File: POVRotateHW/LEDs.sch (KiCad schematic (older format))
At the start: 8 parts

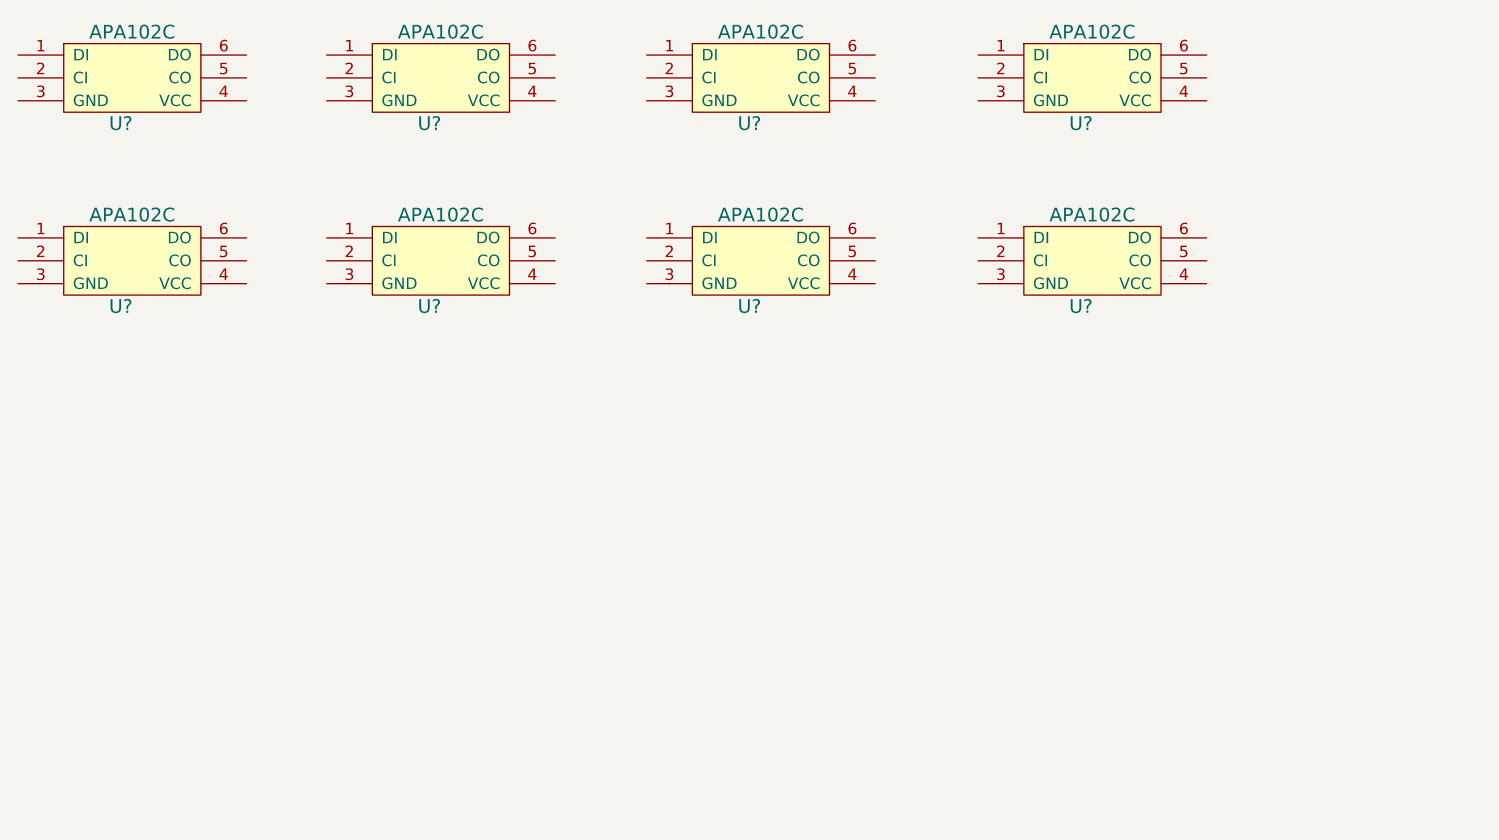
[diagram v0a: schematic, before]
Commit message: Connected some pins up.
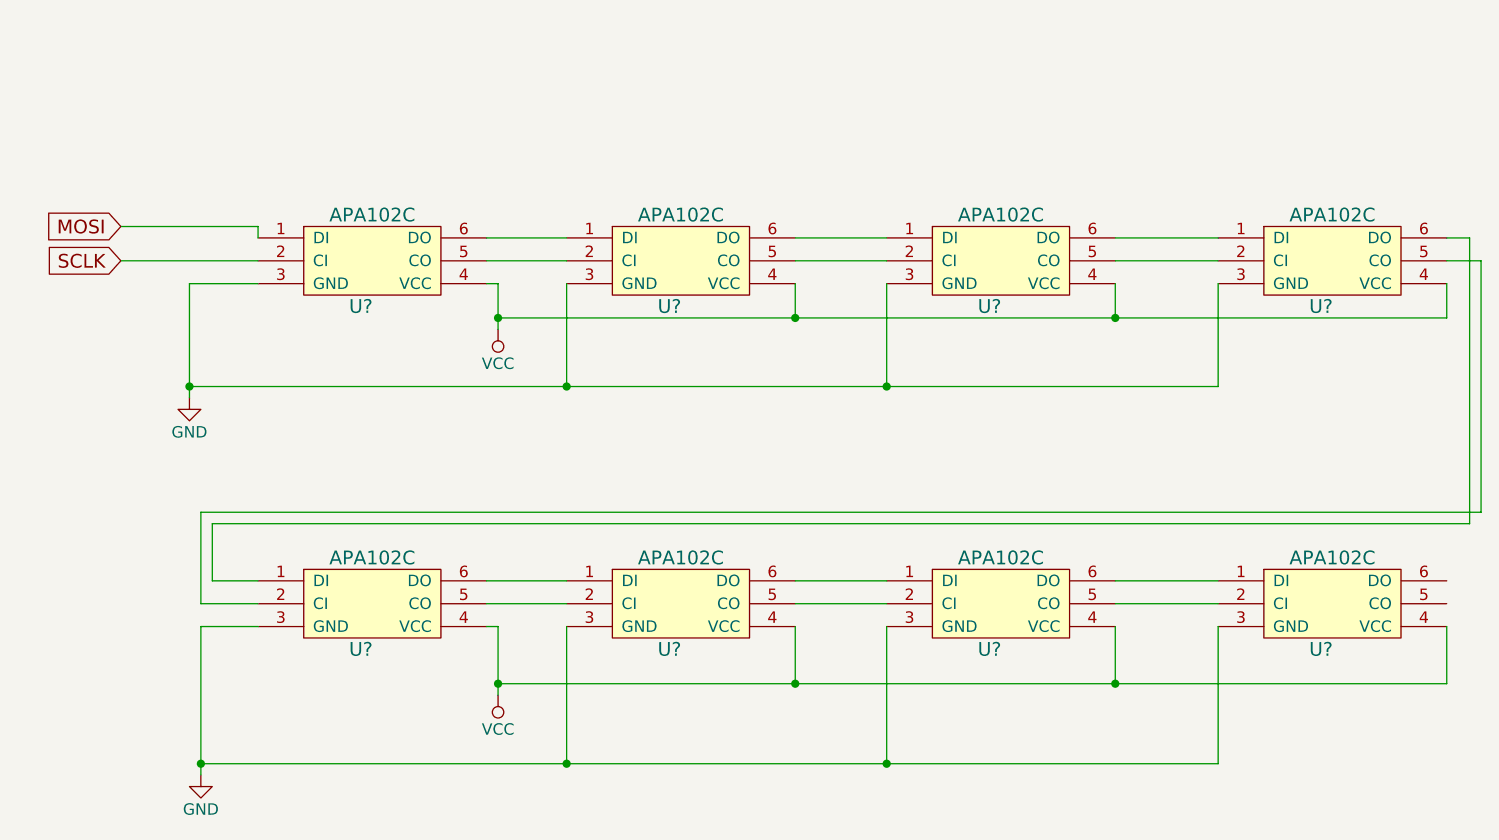
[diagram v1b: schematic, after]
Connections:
- net MOSI: now reaches U?.1 (DI)
- net SCLK: now reaches U?.2 (CI)
- net GND: now reaches U?.3 (GND)
- net GND: now also U?.3 (GND), U?.3 (GND), U?.3 (GND), U?.3 (GND), U?.3 (GND), U?.3 (GND), U?.3 (GND)
- net VCC: now reaches U?.4 (VCC)
- net VCC: now also U?.4 (VCC), U?.4 (VCC), U?.4 (VCC), U?.4 (VCC), U?.4 (VCC), U?.4 (VCC), U?.4 (VCC)
- net at U?.5 (CO): now also U?.2 (CI) (x7)
- net at U?.6 (DO): now also U?.1 (DI) (x7)
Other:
- moved on the sheet: U?

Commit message: Finished the schematic for the POVRotate system, started on layout.
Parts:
- gave numbers to parts that had none: 8
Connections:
- no-connect marks 0 -> 2
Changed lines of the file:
@@
 $EndDescr
 $Comp
-L APA102C U?
+L APA102C U5
 U 1 1 58127307
 P 4300 2700
-F 0 "U?" H 4250 2500 60  0000 C CNN
+F 0 "U5" H 4250 2500 60  0000 C CNN
 F 1 "APA102C" H 4300 2900 60  0000 C CNN
 F 2 "" H 4350 2650 60  0001 C CNN
@@
 $EndComp
 $Comp
-L APA102C U?
+L APA102C U7
 U 1 1 58127369
 P 5650 2700
-F 0 "U?" H 5600 2500 60  0000 C CNN
+F 0 "U7" H 5600 2500 60  0000 C CNN
 F 1 "APA102C" H 5650 2900 60  0000 C CNN
 F 2 "" H 5700 2650 60  0001 C CNN
@@
 $EndComp
 $Comp
-L APA102C U?
+L APA102C U9
 U 1 1 581273A7
 P 7050 2700
-F 0 "U?" H 7000 2500 60  0000 C CNN
+F 0 "U9" H 7000 2500 60  0000 C CNN
 F 1 "APA102C" H 7050 2900 60  0000 C CNN
 F 2 "" H 7100 2650 60  0001 C CNN
@@
 $EndComp
 $Comp
-L APA102C U?
+L APA102C U11
 U 1 1 581273F0
 P 8500 2700
-F 0 "U?" H 8450 2500 60  0000 C CNN
+F 0 "U11" H 8450 2500 60  0000 C CNN
 F 1 "APA102C" H 8500 2900 60  0000 C CNN
 F 2 "" H 8550 2650 60  0001 C CNN
@@
 $EndComp
 $Comp
-L APA102C U?
+L APA102C U6
 U 1 1 58127436
 P 4300 4200
-F 0 "U?" H 4250 4000 60  0000 C CNN
+F 0 "U6" H 4250 4000 60  0000 C CNN
 F 1 "APA102C" H 4300 4400 60  0000 C CNN
 F 2 "" H 4350 4150 60  0001 C CNN
@@
 $EndComp
 $Comp
-L APA102C U?
+L APA102C U8
 U 1 1 581274C5
 P 5650 4200
-F 0 "U?" H 5600 4000 60  0000 C CNN
+F 0 "U8" H 5600 4000 60  0000 C CNN
 F 1 "APA102C" H 5650 4400 60  0000 C CNN
 F 2 "" H 5700 4150 60  0001 C CNN
@@
 $EndComp
 $Comp
-L APA102C U?
+L APA102C U10
 U 1 1 5812751F
 P 7050 4200
-F 0 "U?" H 7000 4000 60  0000 C CNN
+F 0 "U10" H 7000 4000 60  0000 C CNN
 F 1 "APA102C" H 7050 4400 60  0000 C CNN
 F 2 "" H 7100 4150 60  0001 C CNN
@@
 $EndComp
 $Comp
-L APA102C U?
+L APA102C U12
 U 1 1 58127568
 P 8500 4200
-F 0 "U?" H 8450 4000 60  0000 C CNN
+F 0 "U12" H 8450 4000 60  0000 C CNN
 F 1 "APA102C" H 8500 4400 60  0000 C CNN
 F 2 "" H 8550 4150 60  0001 C CNN
@@
 SCLK
 $Comp
-L VCC #PWR?
+L VCC #PWR032
 U 1 1 5814D242
 P 4850 3000
-F 0 "#PWR?" H 4850 2850 50  0001 C CNN
+F 0 "#PWR032" H 4850 2850 50  0001 C CNN
 F 1 "VCC" H 4850 3150 50  0000 C CNN
 F 2 "" H 4850 3000 50  0000 C CNN
@@
 $EndComp
 $Comp
-L GND #PWR?
+L GND #PWR033
 U 1 1 5814D248
 P 3500 3300
-F 0 "#PWR?" H 3500 3050 50  0001 C CNN
+F 0 "#PWR033" H 3500 3050 50  0001 C CNN
 F 1 "GND" H 3500 3150 50  0000 C CNN
 F 2 "" H 3500 3300 50  0000 C CNN
@@
 $EndComp
 $Comp
-L GND #PWR?
+L GND #PWR034
 U 1 1 5814D2A4
 P 3550 4950
-F 0 "#PWR?" H 3550 4700 50  0001 C CNN
+F 0 "#PWR034" H 3550 4700 50  0001 C CNN
 F 1 "GND" H 3550 4800 50  0000 C CNN
 F 2 "" H 3550 4950 50  0000 C CNN
@@
 Connection ~ 7550 2950
 $Comp
-L VCC #PWR?
+L VCC #PWR035
 U 1 1 5814D854
 P 4850 4600
-F 0 "#PWR?" H 4850 4450 50  0001 C CNN
+F 0 "#PWR035" H 4850 4450 50  0001 C CNN
 F 1 "VCC" H 4850 4750 50  0000 C CNN
 F 2 "" H 4850 4600 50  0000 C CNN
@@
 	9000 4550 9000 4300
 Connection ~ 7550 4550
+NoConn ~ 9000 4100
+NoConn ~ 9000 4200
 $EndSCHEMATC

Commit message: Started work on the POV Rotate layout.
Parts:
- U10, U11, U12, U5, U6, U7, U8, U9: footprint (none) -> KicadLibrary:LED_5050
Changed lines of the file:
@@
 F 0 "U5" H 4250 2500 60  0000 C CNN
 F 1 "APA102C" H 4300 2900 60  0000 C CNN
-F 2 "" H 4350 2650 60  0001 C CNN
+F 2 "KicadLibrary:LED_5050" H 4350 2650 60  0001 C CNN
 F 3 "" H 4350 2650 60  0001 C CNN
 	1    4300 2700
@@
 F 0 "U7" H 5600 2500 60  0000 C CNN
 F 1 "APA102C" H 5650 2900 60  0000 C CNN
-F 2 "" H 5700 2650 60  0001 C CNN
+F 2 "KicadLibrary:LED_5050" H 5700 2650 60  0001 C CNN
 F 3 "" H 5700 2650 60  0001 C CNN
 	1    5650 2700
@@
 F 0 "U9" H 7000 2500 60  0000 C CNN
 F 1 "APA102C" H 7050 2900 60  0000 C CNN
-F 2 "" H 7100 2650 60  0001 C CNN
+F 2 "KicadLibrary:LED_5050" H 7100 2650 60  0001 C CNN
 F 3 "" H 7100 2650 60  0001 C CNN
 	1    7050 2700
@@
 F 0 "U11" H 8450 2500 60  0000 C CNN
 F 1 "APA102C" H 8500 2900 60  0000 C CNN
-F 2 "" H 8550 2650 60  0001 C CNN
+F 2 "KicadLibrary:LED_5050" H 8550 2650 60  0001 C CNN
 F 3 "" H 8550 2650 60  0001 C CNN
 	1    8500 2700
@@
 F 0 "U6" H 4250 4000 60  0000 C CNN
 F 1 "APA102C" H 4300 4400 60  0000 C CNN
-F 2 "" H 4350 4150 60  0001 C CNN
+F 2 "KicadLibrary:LED_5050" H 4350 4150 60  0001 C CNN
 F 3 "" H 4350 4150 60  0001 C CNN
 	1    4300 4200
@@
 F 0 "U8" H 5600 4000 60  0000 C CNN
 F 1 "APA102C" H 5650 4400 60  0000 C CNN
-F 2 "" H 5700 4150 60  0001 C CNN
+F 2 "KicadLibrary:LED_5050" H 5700 4150 60  0001 C CNN
 F 3 "" H 5700 4150 60  0001 C CNN
 	1    5650 4200
@@
 F 0 "U10" H 7000 4000 60  0000 C CNN
 F 1 "APA102C" H 7050 4400 60  0000 C CNN
-F 2 "" H 7100 4150 60  0001 C CNN
+F 2 "KicadLibrary:LED_5050" H 7100 4150 60  0001 C CNN
 F 3 "" H 7100 4150 60  0001 C CNN
 	1    7050 4200
@@
 F 0 "U12" H 8450 4000 60  0000 C CNN
 F 1 "APA102C" H 8500 4400 60  0000 C CNN
-F 2 "" H 8550 4150 60  0001 C CNN
+F 2 "KicadLibrary:LED_5050" H 8550 4150 60  0001 C CNN
 F 3 "" H 8550 4150 60  0001 C CNN
 	1    8500 4200

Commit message: Updated the designs ref des to the LEDs work.
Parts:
- renumbered U8 to U10, U10 to U11, U7 to U6, U9 to U7, U11 to U8, U6 to U9
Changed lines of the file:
@@
 $EndComp
 $Comp
-L APA102C U7
+L APA102C U6
 U 1 1 58127369
 P 5650 2700
-F 0 "U7" H 5600 2500 60  0000 C CNN
+F 0 "U6" H 5600 2500 60  0000 C CNN
 F 1 "APA102C" H 5650 2900 60  0000 C CNN
 F 2 "KicadLibrary:LED_5050" H 5700 2650 60  0001 C CNN
@@
 $EndComp
 $Comp
-L APA102C U9
+L APA102C U7
 U 1 1 581273A7
 P 7050 2700
-F 0 "U9" H 7000 2500 60  0000 C CNN
+F 0 "U7" H 7000 2500 60  0000 C CNN
 F 1 "APA102C" H 7050 2900 60  0000 C CNN
 F 2 "KicadLibrary:LED_5050" H 7100 2650 60  0001 C CNN
@@
 $EndComp
 $Comp
-L APA102C U11
+L APA102C U8
 U 1 1 581273F0
 P 8500 2700
-F 0 "U11" H 8450 2500 60  0000 C CNN
+F 0 "U8" H 8450 2500 60  0000 C CNN
 F 1 "APA102C" H 8500 2900 60  0000 C CNN
 F 2 "KicadLibrary:LED_5050" H 8550 2650 60  0001 C CNN
@@
 $EndComp
 $Comp
-L APA102C U6
+L APA102C U9
 U 1 1 58127436
 P 4300 4200
-F 0 "U6" H 4250 4000 60  0000 C CNN
+F 0 "U9" H 4250 4000 60  0000 C CNN
 F 1 "APA102C" H 4300 4400 60  0000 C CNN
 F 2 "KicadLibrary:LED_5050" H 4350 4150 60  0001 C CNN
@@
 $EndComp
 $Comp
-L APA102C U8
+L APA102C U10
 U 1 1 581274C5
 P 5650 4200
-F 0 "U8" H 5600 4000 60  0000 C CNN
+F 0 "U10" H 5600 4000 60  0000 C CNN
 F 1 "APA102C" H 5650 4400 60  0000 C CNN
 F 2 "KicadLibrary:LED_5050" H 5700 4150 60  0001 C CNN
@@
 $EndComp
 $Comp
-L APA102C U10
+L APA102C U11
 U 1 1 5812751F
 P 7050 4200
-F 0 "U10" H 7000 4000 60  0000 C CNN
+F 0 "U11" H 7000 4000 60  0000 C CNN
 F 1 "APA102C" H 7050 4400 60  0000 C CNN
 F 2 "KicadLibrary:LED_5050" H 7100 4150 60  0001 C CNN

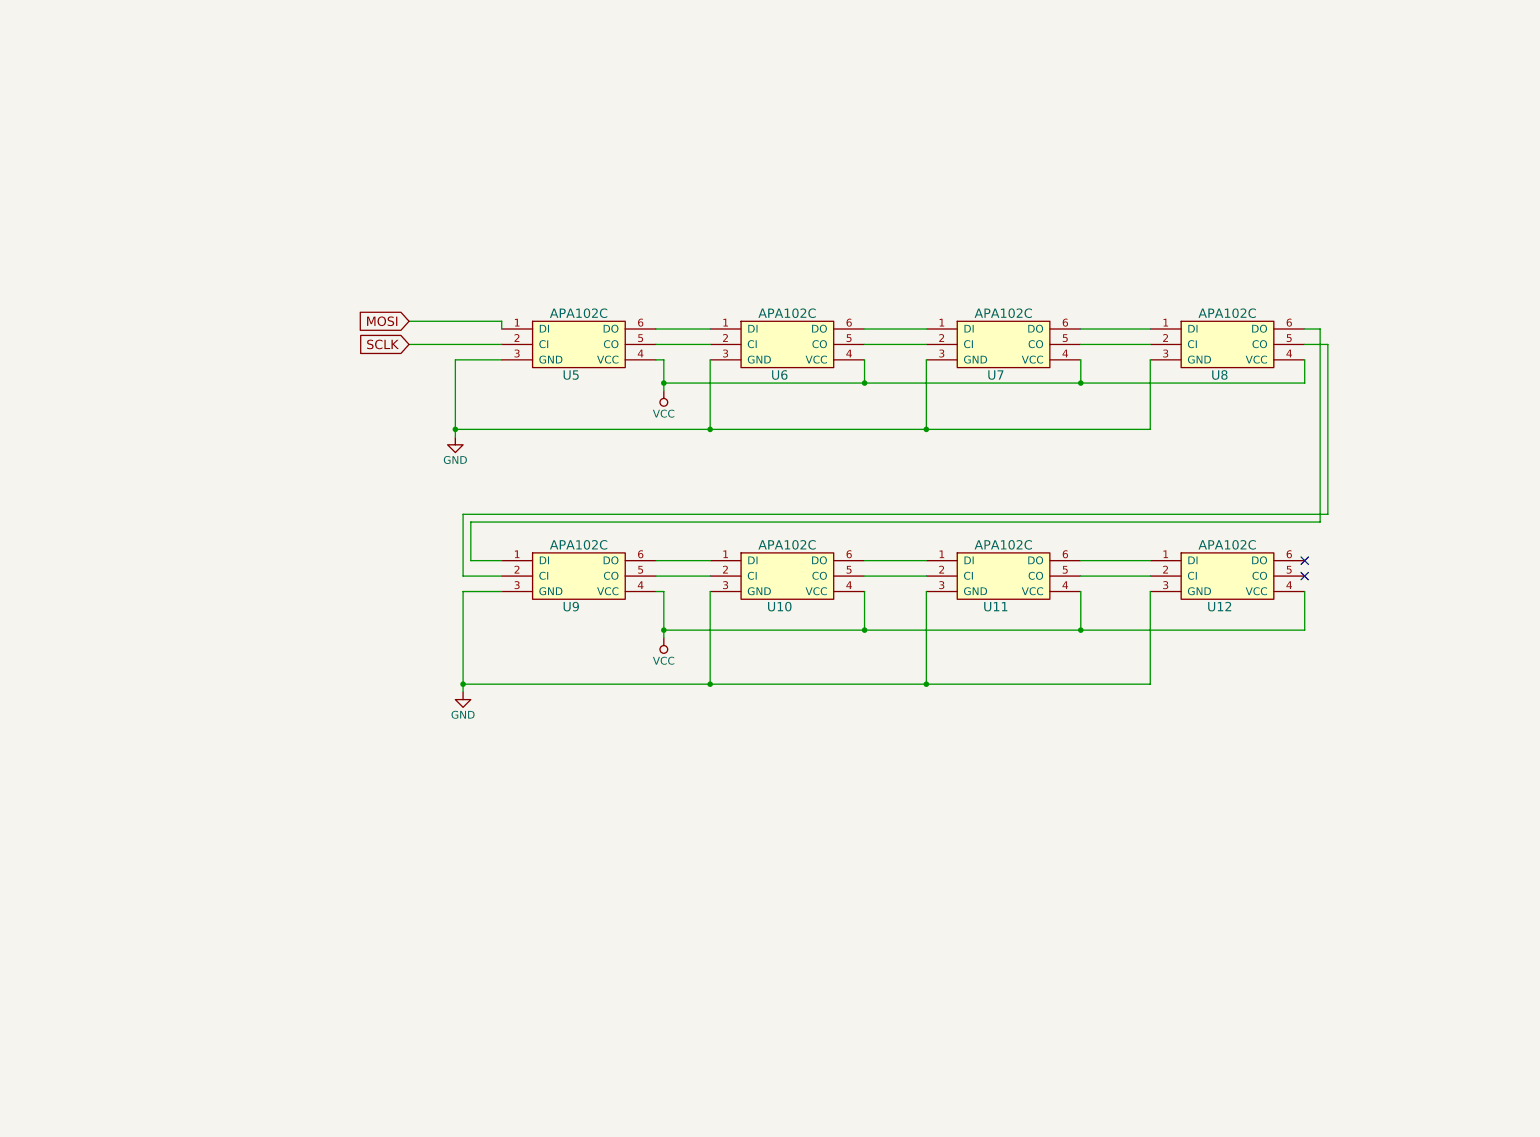
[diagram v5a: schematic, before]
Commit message: Rerouting board for RevB
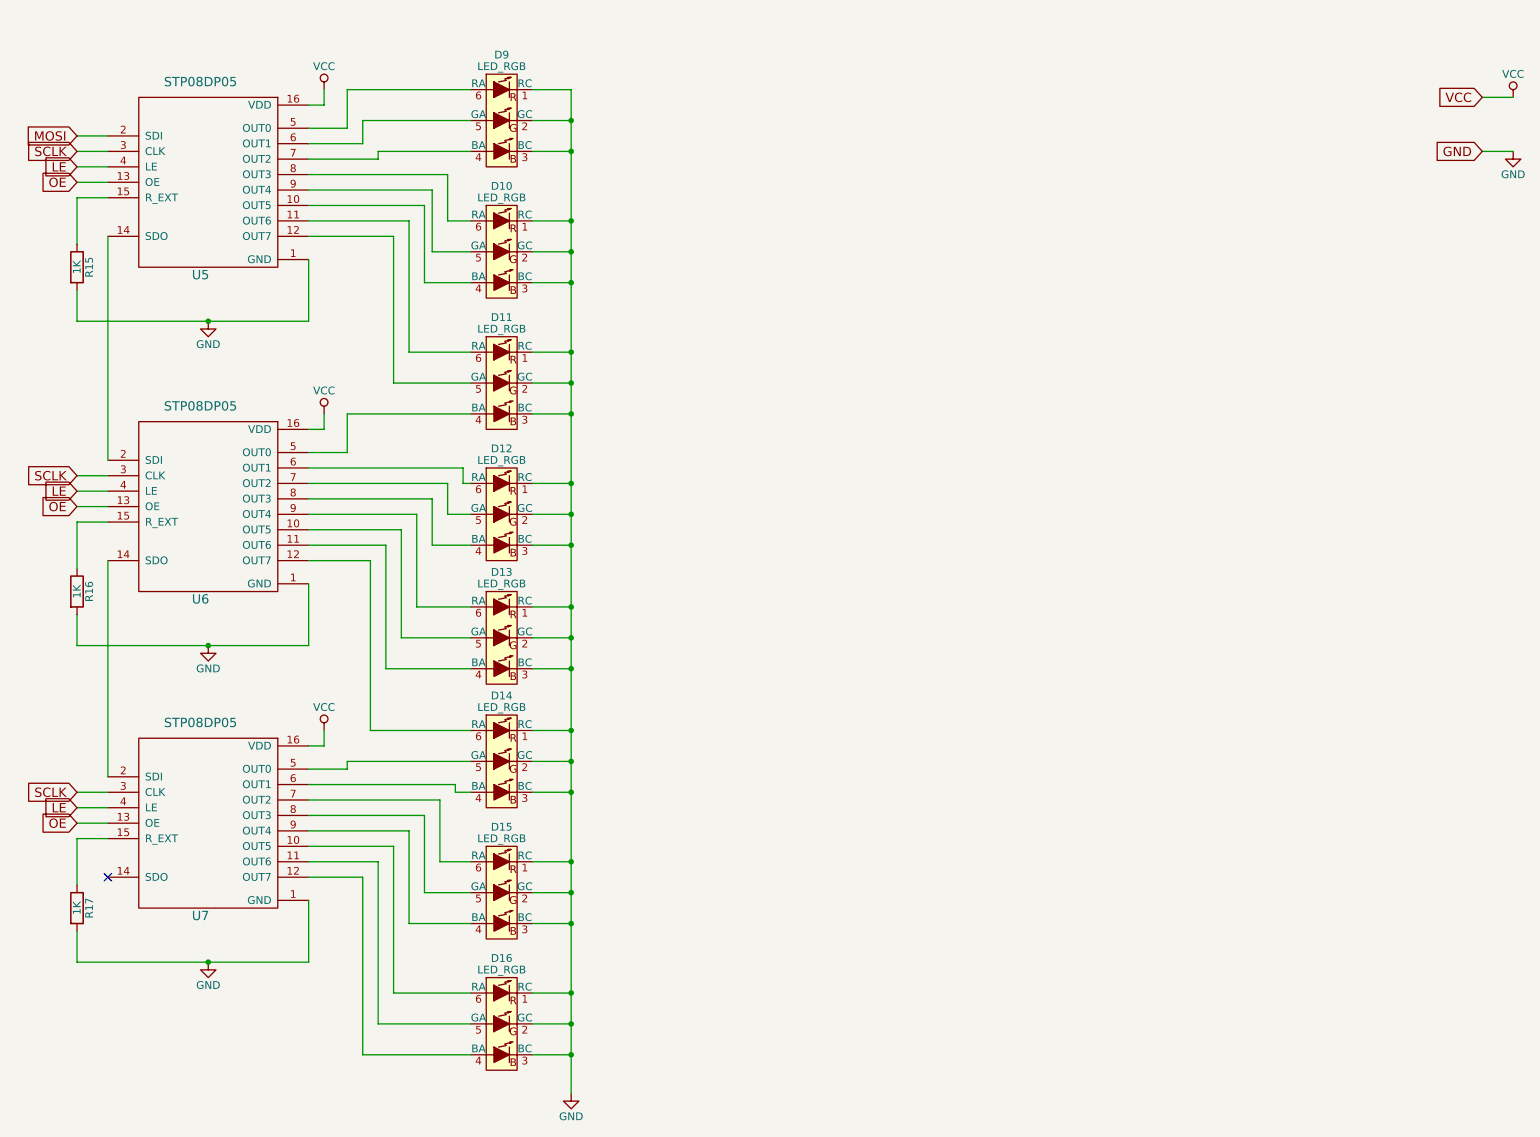
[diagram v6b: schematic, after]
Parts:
- removed U10, U11, U12, U5, U6, U7, U8, U9: APA102C, KicadLibrary:LED_5050, symbol APA102C
- added D10, D11, D12, D13, D14, D15, D16, D9: LED_RGB, LEDs:LED_RGB_PLLC-6, symbol LED_RGB
- added R15, R16, R17: 1K, Resistors_SMD:R_0805, symbol R
- added U5, U6, U7: STP08DP05, SMD_Packages:SO-16-N, symbol STP08DP05
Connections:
- net GND: now also D10.1 (RC), D10.2 (GC), D10.3 (BC), D11.1 (RC), D11.2 (GC), D11.3 (BC), D12.1 (RC), D12.2 (GC), D12.3 (BC), D13.1 (RC), D13.2 (GC), D13.3 (BC), D14.1 (RC), D14.2 (GC), D14.3 (BC), D15.1 (RC), D15.2 (GC), D15.3 (BC), D16.1 (RC), D16.2 (GC), D16.3 (BC), D9.1 (RC), D9.2 (GC), D9.3 (BC), R15.2, R16.2, R17.2, U5.1 (GND), U6.1 (GND), U7.1 (GND)
- net MOSI: now also U5.2 (SDI)
- net SCLK: now also U5.3 (CLK), U6.3 (CLK), U7.3 (CLK)
- net VCC: now also U5.16 (VDD), U6.16 (VDD), U7.16 (VDD)
- new net: D10.4 (BA), U5.10 (OUT5)
- new net: D11.6 (RA), U5.11 (OUT6)
- new net: D11.5 (GA), U5.12 (OUT7)
- new net: U5.14 (SDO), U6.2 (SDI)
- new net: R15.1, U5.15 (R_EXT)
- new net: D9.6 (RA), U5.5 (OUT0)
- new net: D9.5 (GA), U5.6 (OUT1)
- new net: D9.4 (BA), U5.7 (OUT2)
- new net: D10.6 (RA), U5.8 (OUT3)
- new net: D10.5 (GA), U5.9 (OUT4)
- new net: D13.5 (GA), U6.10 (OUT5)
- new net: D13.4 (BA), U6.11 (OUT6)
- new net: D14.6 (RA), U6.12 (OUT7)
- new net: U6.14 (SDO), U7.2 (SDI)
- new net: R16.1, U6.15 (R_EXT)
- new net: D11.4 (BA), U6.5 (OUT0)
- new net: D12.6 (RA), U6.6 (OUT1)
- new net: D12.5 (GA), U6.7 (OUT2)
- new net: D12.4 (BA), U6.8 (OUT3)
- new net: D13.6 (RA), U6.9 (OUT4)
- new net: D16.6 (RA), U7.10 (OUT5)
- new net: D16.5 (GA), U7.11 (OUT6)
- new net: D16.4 (BA), U7.12 (OUT7)
- new net: R17.1, U7.15 (R_EXT)
- new net: D14.5 (GA), U7.5 (OUT0)
- new net: D14.4 (BA), U7.6 (OUT1)
- new net: D15.6 (RA), U7.7 (OUT2)
- new net: D15.5 (GA), U7.8 (OUT3)
- new net: D15.4 (BA), U7.9 (OUT4)
- new net LE: U5.4 (LE), U6.4 (LE), U7.4 (LE)
- new net OE: U5.13 (OE), U6.13 (OE), U7.13 (OE)
- no-connect marks 2 -> 1
